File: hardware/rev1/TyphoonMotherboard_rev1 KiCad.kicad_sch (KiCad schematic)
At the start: 52 parts, among them J2 Conn_01x04_Pin, J3 USB_C_Receptacle_USB2.0, J4 Conn_01x04_Pin, SW1 SW_Push, SW2 SW_Push, SW3 SW_Push, SW4 SW_Push, SW5 SW_Push, U1 MCP1825S, U2 ESP32-S3-WROOM-1, U3 SN65HVD233, U4 BQ25895RTW

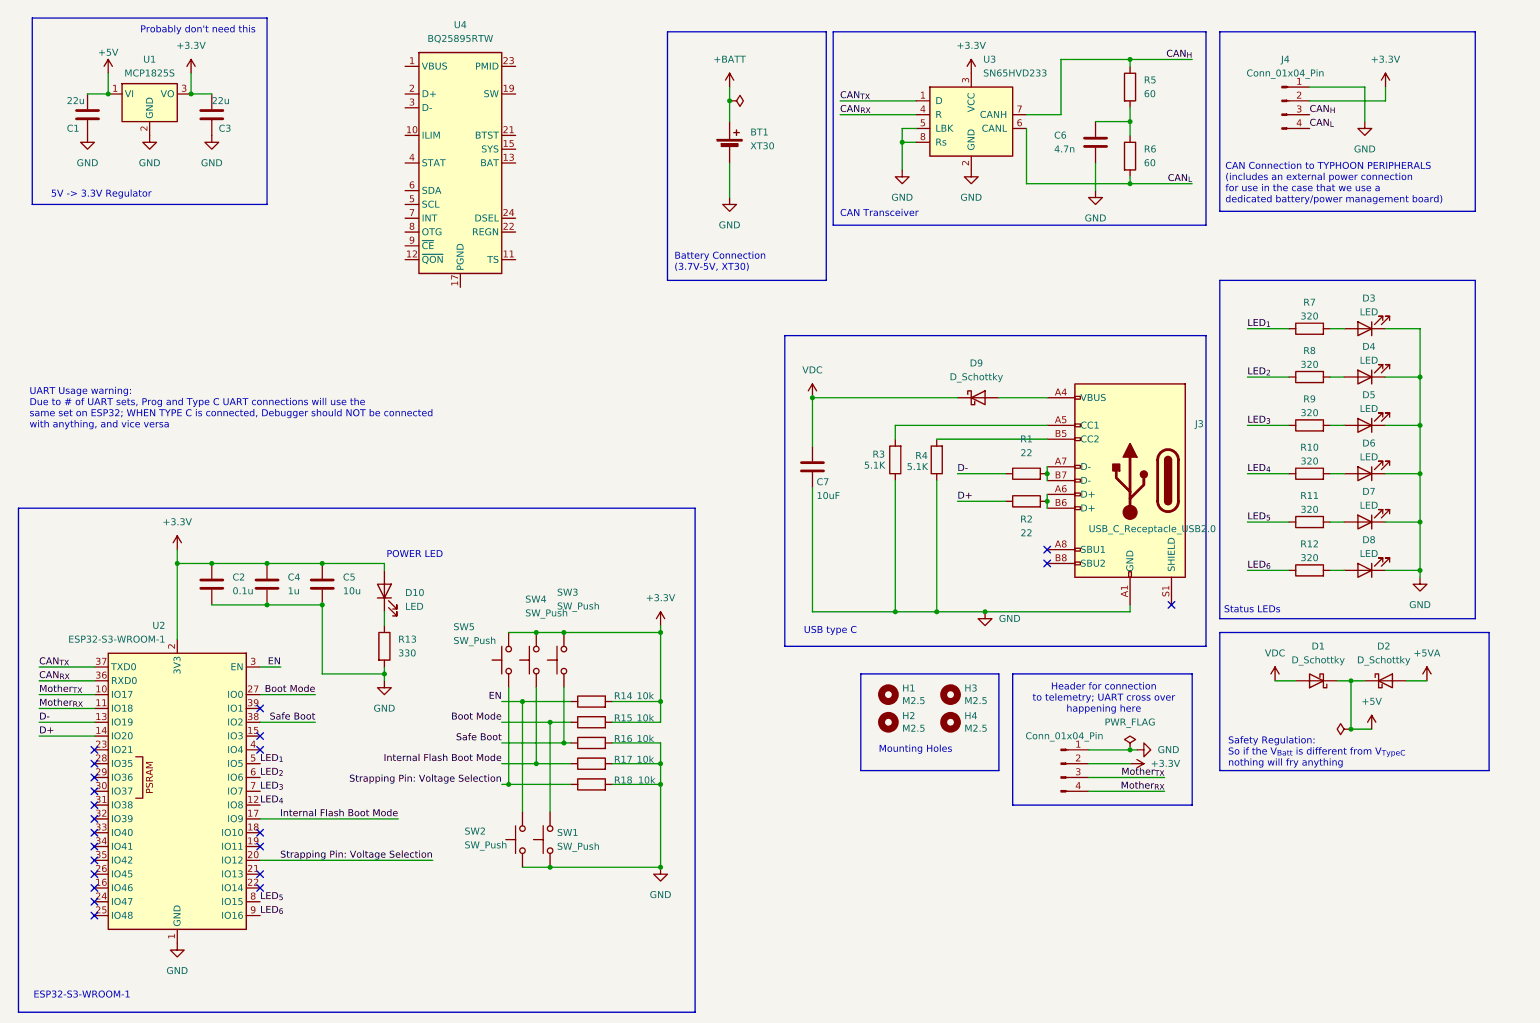
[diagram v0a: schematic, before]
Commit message: Updated Voltage Regulation
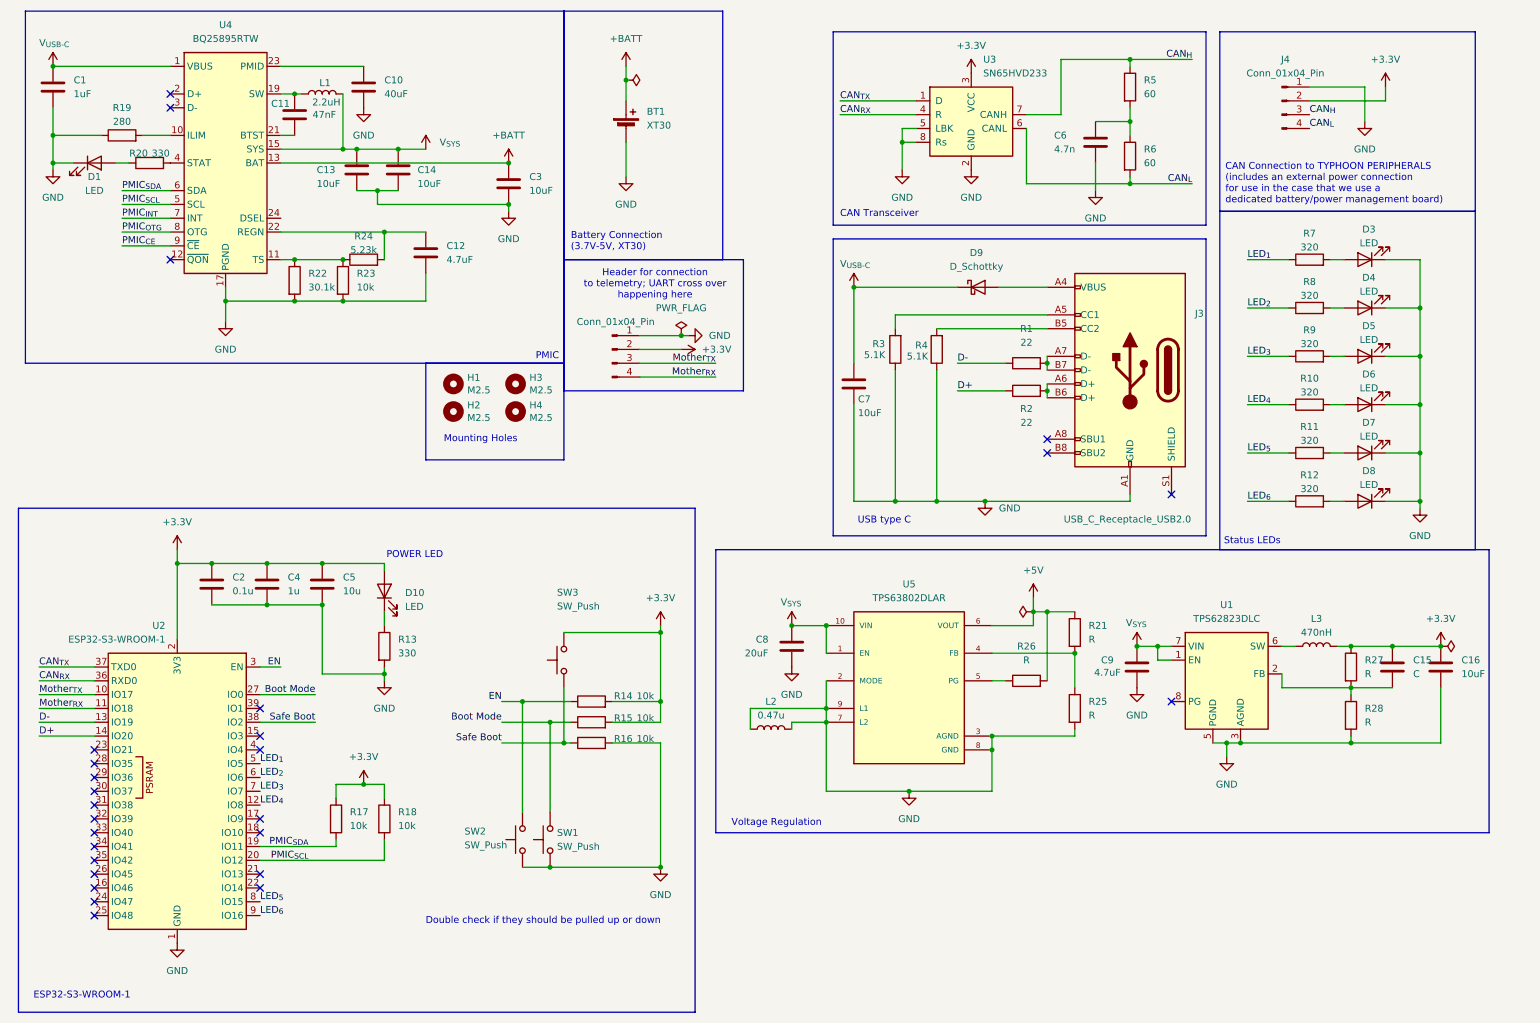
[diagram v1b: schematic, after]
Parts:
- removed D1, D2: D_Schottky, Diode_SMD:D_SOD-123, symbol Device:D_Schottky
- removed SW4, SW5: SW_Push, symbol Switch:SW_Push
- removed U1: MCP1825S, Package_TO_SOT_SMD:SOT-223-3_TabPin2, symbol Regulator_Linear:MCP1825S
- added C10: 40uF, symbol Device:C
- added C11: 47nF, symbol Device:C
- added C12, C9: 4.7uF, symbol Device:C
- added C13, C14, C16: 10uF, symbol Device:C
- added C15: C, symbol Device:C
- added C8: 20uF, symbol Device:C
- added D1: LED, symbol Device:LED
- added L1: 2.2uH, symbol Device:L
- added L2: 0.47u, symbol Device:L
- added L3: 470nH, symbol Device:L
- added R19: 280, symbol Device:R
- added R20: 330, symbol Device:R
- added R21, R25, R26, R27, R28: R, symbol Device:R
- added R22: 30.1k, symbol Device:R
- added R23: 10k, symbol Device:R
- added R24: 5.23k, symbol Device:R
- added U1: TPS62823DLC, Package_SON:Texas_VSON-HR-8_1.5x2mm_P0.5mm, symbol Regulator_Switching:TPS62823DLC
- added U5: TPS63802DLAR, TPS63802DLAR:VREG_TPS63802DLAR, symbol TPS63802DLAR:TPS63802DLAR
- C1: value 22u -> 1uF; footprint Capacitor_SMD:C_0603_1608Metric -> (none)
- C3: value 22u -> 10uF; footprint Capacitor_SMD:C_0603_1608Metric -> (none)
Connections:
- net VDC is gone; now on net V_{USB-C}: C7.1, D9.1 (K)
- net +3.3V: now also R17.1, R18.1, C15.1, C16.1, L3.2, R27.1; no longer C3.2
- net +5V: now also R21.1, R26.2, U5.6 (VOUT); no longer C1.2
- net +BATT: now also C3.1, U4.13 (BAT), U4.14 (BAT)
- net GND: now also C1.2, C3.2, U4.17 (PGND), U4.18 (PGND), U4.25 (PGND), C10.2, C12.2, C13.2, C14.2, C16.2, C8.2, C9.2, D1.1 (K), L2.1, L2.2, R19.1, R22.2, R23.2, R25.2, R28.2, U1.3 (AGND), U1.5 (PGND), U5.2 (MODE), U5.3 (AGND), U5.7 (L2), U5.8 (GND), U5.9 (L1); no longer C1.1, C3.1, R17.2, R18.2
- net V_{USB-C}: now reaches U4.1 (VBUS)
- net V_{USB-C}: now also C1.1
- net at U4.10 (ILIM): now also R19.2
- net at U4.11 (TS): now also R22.1, R23.1, R24.1
- net V_{SYS}: now reaches U4.15 (SYS), U4.16 (SYS)
- net V_{SYS}: now also C13.1, C14.1, C8.1, C9.1, L1.2, U1.1 (EN), U1.7 (VIN), U5.1 (EN), U5.10 (VIN)
- net at U4.19 (SW), U4.20 (SW): now also C11.1, L1.1
- net at U4.21 (BTST): now also C11.2
- net at U4.22 (REGN): now also C12.1, R24.2
- net at U4.23 (PMID): now also C10.1
- net at U4.4 (STAT): now also R20.2
- net PMIC_{SCL}: now reaches U4.5 (SCL)
- net PMIC_{SCL}: now also R18.2, U2.20 (IO12)
- net PMIC_{SDA}: now reaches U4.6 (SDA)
- net PMIC_{SDA}: now also R17.2, U2.19 (IO11)
- net PMIC_{INT}: now reaches U4.7 (INT)
- net PMIC_{OTG}: now reaches U4.8 (OTG)
- net PMIC_{CE}: now reaches U4.9 (~{CE})
- net Internal Flash Boot Mode: no longer names the net of U2.17 (IO9)
- net Internal Flash Boot Mode: no longer R17.1
- removed net Strapping Pin: Voltage Selection: R18.1, U2.20 (IO12)
- new net: D1.2 (A), R20.1
- new net: C15.2, R27.2, R28.1, U1.2 (FB)
- new net: L3.1, U1.6 (SW)
- new net: R26.1, U5.5 (PG)
- new net: R21.2, R25.1, U5.4 (FB)
- no-connect marks 23 -> 27
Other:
- note added: "Double check if they should be pulled up or down"
- note added: "PMIC"
- note added: "Voltage Regulation"
- note removed: "5V -> 3.3V Regulator"
- note removed: "Probably don't need this"
- note removed: "Safety Regulation: So if the V_{Batt} is different from V_{TypeC} nothing will fry anything"
- note removed: "UART Usage warning: Due to # of UART sets, Prog and Type C UART connections will use the same set on ESP32; WHEN TYPE C is connected, Debugger should NOT be connected with anything, and vice versa"
- moved on the sheet: BT1, C7, D3, D4, D5, D6, D7, D8, D9, H1, H2, H3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

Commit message: Rev1 Fully Finalized
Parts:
- removed C7: 10uF, symbol Device:C
- removed D7, D8: LED, LED_SMD:LED_0805_2012Metric, symbol Device:LED
- removed D9: D_Schottky, symbol Device:D_Schottky
- removed J3: USB_C_Receptacle_USB2.0, Connector_USB:USB_C_Receptacle_HRO_TYPE-C-31-M-12, symbol Connector:USB_C_Receptacle_USB2.0_16P
- removed J4: Conn_01x04_Pin, Connector_JST:JST_EH_S4B-EH_1x04_P2.50mm_Horizontal, symbol Connector:Conn_01x04_Pin
- removed R23: 10k, symbol Device:R
- removed R3, R4: 5.1K, Resistor_SMD:R_0603_1608Metric, symbol Device:R
- removed U1: TPS62823DLC, Package_SON:Texas_VSON-HR-8_1.5x2mm_P0.5mm, symbol Regulator_Switching:TPS62823DLC
- added C17: 22uF, Capacitor_SMD:C_0603_1608Metric, symbol Device:C
- added C18: 10uF, Capacitor_SMD:C_0603_1608Metric, symbol Device:C
- added D8: SMBJ5.0A, SMBJ5.0A:DIOM4336X265N, symbol SMBJ5.0A:SMBJ5.0A
- added J1: Conn_02x04_Odd_Even, Connector_PinSocket_2.54mm:PinSocket_2x04_P2.54mm_Vertical, symbol Connector_Generic:Conn_02x04_Odd_Even
- added J3: UJ20-C-H-C-4-SMT-TR, UJ20-C-H-C-4-SMT-TR:CUI_UJ20-C-H-C-4-SMT-TR, symbol UJ20-C-H-C-4-SMT-TR:UJ20-C-H-C-4-SMT-TR
- added J5, J6: Conn_01x02_Pin, Connector_JST:JST_XH_B2B-XH-A_1x02_P2.50mm_Vertical, symbol Connector:Conn_01x02_Pin
- added J7: Conn_01x04_Pin, Connector_JST:JST_XH_B4B-XH-A_1x04_P2.50mm_Vertical, symbol Connector:Conn_01x04_Pin
- added R29: 91k, Resistor_SMD:R_0603_1608Metric, symbol Device:R
- added RT1: 103AT-2, 103AT-2:103AT-2, symbol 103AT-2:103AT-2
- added U1: USBLC6-2SC6, Package_TO_SOT_SMD:SOT-23-6, symbol Power_Protection:USBLC6-2SC6
- added U6: TPS63802DLAR, TPS63802DLAR (1):VREG_TPS63802DLAR, symbol TPS63802DLAR:TPS63802DLAR
- BT1: footprint Connector_AMASS:AMASS_XT30PW-M_1x02_P2.50mm_Horizontal -> Connector_AMASS:AMASS_XT30U-F_1x02_P5.0mm_Vertical
- C1, C11, C12, C13, C14, C3: footprint (none) -> Capacitor_SMD:C_0603_1608Metric
- C10: value 40uF -> 47uF; footprint (none) -> Capacitor_SMD:C_0603_1608Metric
- C15: value C -> 100nF; footprint (none) -> Capacitor_SMD:C_0603_1608Metric
- C16: value 10uF -> 22uF; footprint (none) -> Capacitor_SMD:C_0603_1608Metric
- C8: value 20uF -> 10uF; footprint (none) -> Capacitor_SMD:C_0603_1608Metric
- C9: value 4.7uF -> 10uF; footprint (none) -> Capacitor_SMD:C_0603_1608Metric
- D1, D10: footprint (none) -> LED_SMD:LED_0805_2012Metric
- J2: footprint Connector_PinHeader_1.27mm:PinHeader_1x04_P1.27mm_Vertical -> Connector_JST:JST_XH_B4B-XH-A_1x04_P2.50mm_Vertical
- L1: footprint (none) -> Inductor_SMD:L_0805_2012Metric
- L2: value 0.47u -> 0.47uH; footprint (none) -> Inductor_SMD:L_0603_1608Metric
- L3: value 470nH -> 0.47uH; footprint (none) -> Inductor_SMD:L_0603_1608Metric
- R1, R2: value 22 -> 10k; footprint (none) -> Resistor_SMD:R_0603_1608Metric
- R11: value 320 -> 10k
- R12: value 320 -> 5.1K
- R13, R14, R15, R16, R17, R18, R19, R20, R24: footprint (none) -> Resistor_SMD:R_0603_1608Metric
- R21: value R -> 511k; footprint (none) -> Resistor_SMD:R_0603_1608Metric
- R22: value 30.1k -> 5.1K; footprint (none) -> Resistor_SMD:R_0603_1608Metric
- R25: value R -> 91k; footprint (none) -> Resistor_SMD:R_0603_1608Metric
- R26, R27: value R -> 100k; footprint (none) -> Resistor_SMD:R_0603_1608Metric
- R28: value R -> 806k; footprint (none) -> Resistor_SMD:R_0603_1608Metric
- SW1, SW2, SW3: footprint (none) -> Connector_PinHeader_2.54mm:PinHeader_1x02_P2.54mm_Vertical
- U5: footprint TPS63802DLAR:VREG_TPS63802DLAR -> TPS63802DLAR (1):VREG_TPS63802DLAR; Description_1 2-A, high-efficient, 11-µA quiescent current buck-boost converter in QFN/DFN package -> 2-A, high-efficient, 11-µA quiescent current buck-boost converter in QFN/DFN package; DigiKey_Part_Number (none) -> 296-TPS63802DLARTR-ND
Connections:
- net +3.3V: now also C15.2, R21.1, U5.6 (VOUT); no longer C15.1, L3.2, R27.1
- net +5V: now also R28.1, C17.1, J5.1 (Pin_1), J6.1 (Pin_1), J7.1 (Pin_1), U6.6 (VOUT); no longer R21.1, R26.2, U5.6 (VOUT)
- net GND: now also C15.1, R12.2, R2.2, R22.1, C17.2, C18.2, D8.A, J3.A12_B1 (GND), J3.A1_B12 (GND), J3.SH1 (SHIELD), J3.SH2 (SHIELD), J3.SH3 (SHIELD), J3.SH4 (SHIELD), J5.2 (Pin_2), J6.2 (Pin_2), J7.2 (Pin_2), R29.2, RT1.1, U1.2 (GND), U6.2 (MODE), U6.3 (AGND), U6.8 (GND); no longer L2.1, L2.2, R22.2, R28.2, U5.7 (L2), U5.9 (L1)
- net PMIC_{CE}: now also R1.2, U2.9 (IO16)
- net PMIC_{INT}: now also R11.2, U2.22 (IO14)
- net PMIC_{OTG}: now also R2.1, U2.8 (IO15)
- net V_{SYS}: now also R26.2, R27.2, U6.1 (EN), U6.10 (VIN)
- net V_{USB-C}: now also R1.1, R11.1, C18.1, D8.C, J3.A4_B9 (VBUS), J3.A9_B4 (VBUS), U1.5 (VBUS)
- net at L3.1: now also U6.9 (L1)
- net at R24.1, U4.11 (TS): now also RT1.2; no longer R22.1
- net PMIC_{NQON}: now reaches U4.12 (~{QON})
- net PMIC_{NQON}: now also U2.21 (IO13)
- net GPIO_{6}: now reaches U2.16 (IO46)
- net GPIO_{6}: now also J1.6 (Pin_6)
- net GPIO_{8}: now reaches U2.24 (IO47)
- net GPIO_{8}: now also J1.8 (Pin_8)
- net GPIO_{7}: now reaches U2.25 (IO48)
- net GPIO_{7}: now also J1.7 (Pin_7)
- net GPIO_{5}: now reaches U2.26 (IO45)
- net GPIO_{5}: now also J1.5 (Pin_5)
- net GPIO_{1}: now reaches U2.32 (IO39)
- net GPIO_{1}: now also J1.1 (Pin_1)
- net GPIO_{2}: now reaches U2.33 (IO40)
- net GPIO_{2}: now also J1.2 (Pin_2)
- net GPIO_{3}: now reaches U2.34 (IO41)
- net GPIO_{3}: now also J1.3 (Pin_3)
- net GPIO_{4}: now reaches U2.35 (IO42)
- net GPIO_{4}: now also J1.4 (Pin_4)
- net CAN_{H} renamed CAN+
- net CAN+: now also J7.4 (Pin_4)
- net CAN_{L} renamed CAN-
- net CAN-: now also J7.3 (Pin_3)
- net D+ renamed D_{MCU}+
- net D_{MCU}+: now also U1.4 (I/O2); no longer R2.1
- net D- renamed D_{MCU}-
- net D_{MCU}-: now also U1.6 (I/O1); no longer R1.1
- removed net LED_{5}: R11.1, U2.8 (IO15)
- net LED_{6}: no longer names the net of R12.1
- net LED_{6}: now also J3.A5 (CC1); no longer U2.9 (IO16)
- new net: L3.2, U6.7 (L2)
- new net: R28.2, R29.1, U6.4 (FB)
- new net: R27.1, U6.5 (PG)
- new net: J3.B5 (CC2), R22.2
- new net: L2.1, U5.9 (L1)
- new net: L2.2, U5.7 (L2)
- new net D_{CONN}+: J3.A6 (DP1), J3.B6 (DP2), U1.3 (I/O2)
- new net D_{CONN}-: J3.A7 (DN1), J3.B7 (DN2), U1.1 (I/O1)
- no-connect marks 27 -> 15
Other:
- note added: "3.3V"
- note added: "5V"
- note added: "Connections to other boards"
- note added: "GPIO pins for future use"
- note added: "USB Data Line Protection IC"
- note removed: "CAN Connection to TYPHOON PERIPHERALS (includes an external power connection for use in the case that we use a dedicated battery/power management board)"
- moved on the sheet: BT1, C8, D3, D4, D5, D6, H1, H2, H3, H4, L2, R10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
